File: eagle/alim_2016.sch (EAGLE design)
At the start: 52 parts, among them J1 AVR_SPI_PRG_6PTH, J2 AVR_SPI_PRG_6PTH, U1 3.3V, U2 LM2678S-5.0, U4 LM2596S-ADJ, U5 ATTINY85-20SU, U6 ATMEGA328P_TQFP

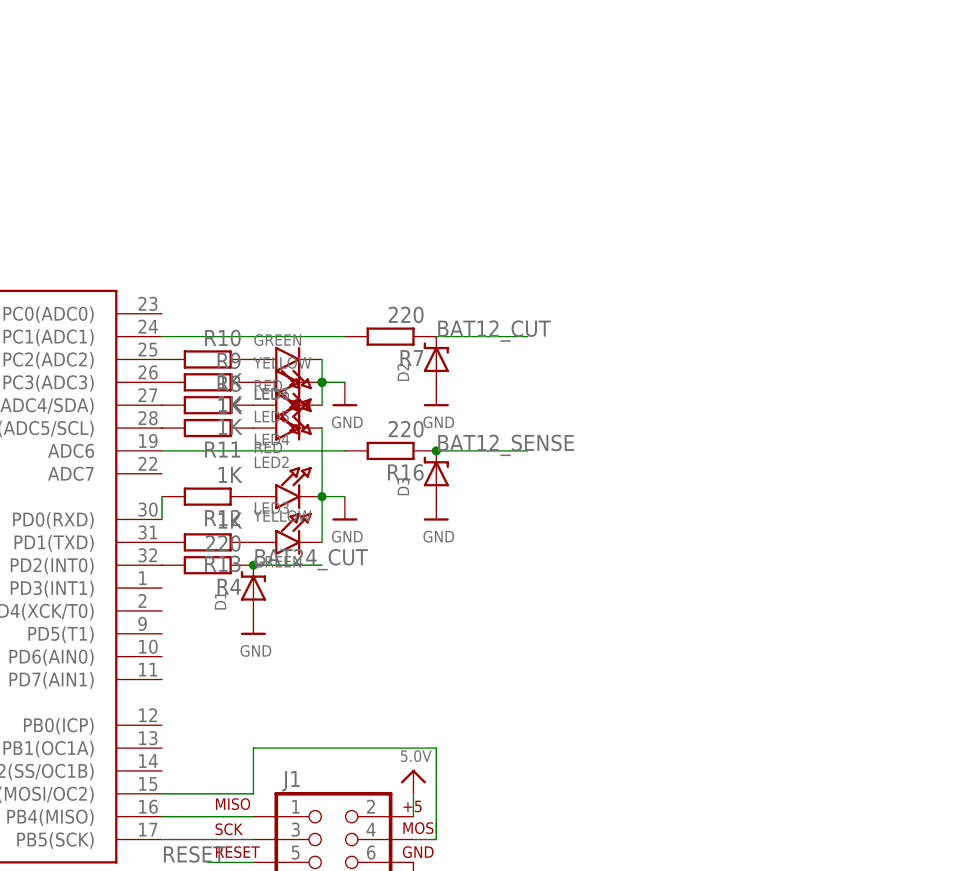
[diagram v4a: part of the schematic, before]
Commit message: adding other battery voltage sense
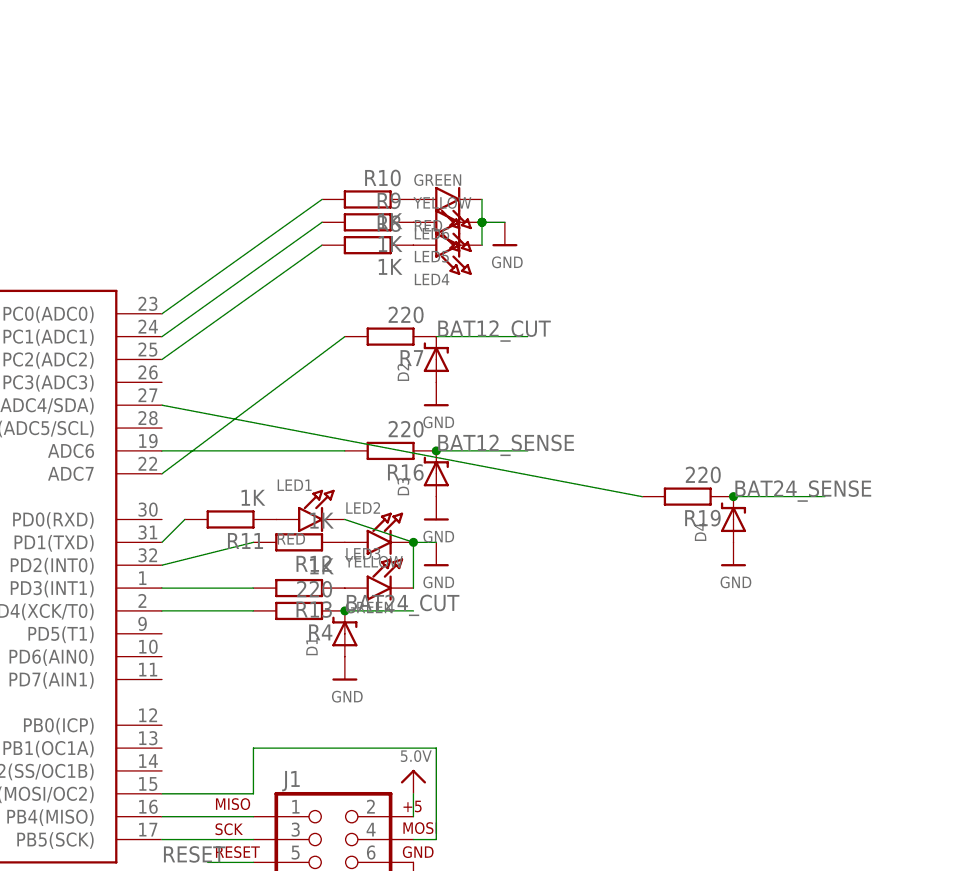
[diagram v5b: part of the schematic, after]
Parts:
- added D4: (no value), alim:DIODE-ZENERSOD123
- added R19: 220, resistor:R-EU_M0805
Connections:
- new net N$28: R19.2, U6.PC4(ADC4/SDA)
- net BAT24_SENSE: now also D4.C, R19.1
- net GND: now also D4.A
- net N$11: now also U6.PD4(XCK/T0); no longer U6.PD2(INT0)
- net N$14: now also R9.2; no longer R7.2
- net N$21: now also R8.2; no longer R10.2
- net N$22: now also R10.2, U6.PC0(ADC0); no longer R9.2, U6.PC3(ADC3)
- net N$23: now also R7.2, U6.ADC7; no longer R8.2, U6.PC4(ADC4/SDA)
- net N$24: now also U6.PD3(INT1); no longer U6.PD1(TXD)
- net N$25: now also U6.PD2(INT0); no longer U6.PD0(RXD)
- net N$26: now also U6.PD1(TXD); no longer U6.PC5(ADC5/SCL)
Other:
- moved on the sheet: D1, LED1, LED2, LED3, LED4, LED5, LED6, R10, R11, R12, R13, R4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
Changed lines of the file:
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@@
 <part name="R17" library="resistor" deviceset="R-EU_" device="M0805" value="1K"/>
 <part name="R18" library="resistor" deviceset="R-EU_" device="M0805" value="1K"/>
+<part name="D4" library="alim" deviceset="DIODE-ZENER" device="SOD123"/>
+<part name="R19" library="resistor" deviceset="R-EU_" device="M0805" value="220"/>
+<part name="U$28" library="microbuilder" deviceset="GND" device=""/>
 </parts>
 <sheets>
@@
 <instance part="12V" gate="-1" x="-2.54" y="43.18"/>
 <instance part="12V" gate="-2" x="-2.54" y="22.86"/>
-<instance part="LED1" gate="G$1" x="109.22" y="-93.98"/>
-<instance part="LED2" gate="G$1" x="109.22" y="-101.6"/>
-<instance part="LED3" gate="G$1" x="109.22" y="-106.68"/>
+<instance part="LED1" gate="G$1" x="111.76" y="-104.14"/>
+<instance part="LED2" gate="G$1" x="119.38" y="-106.68"/>
+<instance part="LED3" gate="G$1" x="119.38" y="-111.76"/>
 <instance part="LED7" gate="G$1" x="-12.7" y="25.4" rot="R270"/>
-<instance part="LED4" gate="G$1" x="109.22" y="-91.44" rot="MR180"/>
-<instance part="LED5" gate="G$1" x="109.22" y="-88.9" rot="MR180"/>
-<instance part="LED6" gate="G$1" x="109.22" y="-86.36" rot="MR180"/>
+<instance part="LED4" gate="G$1" x="127" y="-73.66" rot="MR180"/>
+<instance part="LED5" gate="G$1" x="127" y="-71.12" rot="MR180"/>
+<instance part="LED6" gate="G$1" x="127" y="-68.58" rot="MR180"/>
 <instance part="LED8" gate="G$1" x="5.08" y="-5.08" rot="R270"/>
 <instance part="R6" gate="G$1" x="-17.78" y="30.48" rot="R180"/>
 <instance part="R3" gate="G$1" x="0" y="0" rot="R180"/>
-<instance part="D1" gate="G$1" x="104.14" y="-111.76" rot="R90"/>
-<instance part="R4" gate="G$1" x="99.06" y="-109.22" rot="R180"/>
+<instance part="D1" gate="G$1" x="114.3" y="-116.84" rot="R90"/>
+<instance part="R4" gate="G$1" x="109.22" y="-114.3" rot="R180"/>
 <instance part="D2" gate="G$1" x="124.46" y="-86.36" rot="R90"/>
 <instance part="R7" gate="G$1" x="119.38" y="-83.82" rot="R180"/>
 <instance part="U$6" gate="G$1" x="124.46" y="-91.44"/>
-<instance part="U$18" gate="G$1" x="104.14" y="-116.84"/>
-<instance part="R8" gate="G$1" x="99.06" y="-91.44" rot="MR0"/>
-<instance part="R9" gate="G$1" x="99.06" y="-88.9" rot="MR0"/>
-<instance part="R10" gate="G$1" x="99.06" y="-86.36" rot="MR0"/>
-<instance part="R11" gate="G$1" x="99.06" y="-93.98" rot="R180"/>
-<instance part="R12" gate="G$1" x="99.06" y="-101.6" rot="R180"/>
-<instance part="R13" gate="G$1" x="99.06" y="-106.68" rot="R180"/>
-<instance part="U$26" gate="G$1" x="114.3" y="-104.14"/>
+<instance part="U$18" gate="G$1" x="114.3" y="-121.92"/>
+<instance part="R8" gate="G$1" x="116.84" y="-73.66" rot="MR0"/>
+<instance part="R9" gate="G$1" x="116.84" y="-71.12" rot="MR0"/>
+<instance part="R10" gate="G$1" x="116.84" y="-68.58" rot="MR0"/>
+<instance part="R11" gate="G$1" x="101.6" y="-104.14" rot="R180"/>
+<instance part="R12" gate="G$1" x="109.22" y="-106.68" rot="R180"/>
+<instance part="R13" gate="G$1" x="109.22" y="-111.76" rot="R180"/>
+<instance part="U$26" gate="G$1" x="124.46" y="-109.22"/>
 <instance part="U6" gate="U$1" x="71.12" y="-111.76"/>
 <instance part="R14" gate="G$1" x="-5.08" y="38.1" rot="R90"/>
@@
 <instance part="D3" gate="G$1" x="124.46" y="-99.06" rot="R90"/>
 <instance part="R16" gate="G$1" x="119.38" y="-96.52" rot="R180"/>
-<instance part="U$25" gate="G$1" x="114.3" y="-91.44"/>
+<instance part="U$25" gate="G$1" x="132.08" y="-73.66"/>
 <instance part="U$27" gate="G$1" x="124.46" y="-104.14"/>
 <instance part="R17" gate="G$1" x="-25.4" y="7.62" rot="R90"/>
 <instance part="R18" gate="G$1" x="-25.4" y="-2.54" rot="R90"/>
+<instance part="D4" gate="G$1" x="157.48" y="-104.14" rot="R90"/>
+<instance part="R19" gate="G$1" x="152.4" y="-101.6" rot="R180"/>
+<instance part="U$28" gate="G$1" x="157.48" y="-109.22"/>
 </instances>
 <busses>
@@
 <pinref part="LED3" gate="G$1" pin="C"/>
 <pinref part="LED2" gate="G$1" pin="C"/>
-<wire x1="111.76" y1="-106.68" x2="111.76" y2="-101.6" width="0.1524" layer="91"/>
+<wire x1="121.92" y1="-111.76" x2="121.92" y2="-106.68" width="0.1524" layer="91"/>
 <pinref part="LED1" gate="G$1" pin="C"/>
-<wire x1="111.76" y1="-101.6" x2="111.76" y2="-93.98" width="0.1524" layer="91"/>
+<wire x1="121.92" y1="-106.68" x2="114.3" y2="-104.14" width="0.1524" layer="91"/>
 <pinref part="U$26" gate="G$1" pin="GND"/>
-<wire x1="114.3" y1="-101.6" x2="111.76" y2="-101.6" width="0.1524" layer="91"/>
-<junction x="111.76" y="-101.6"/>
+<wire x1="124.46" y1="-106.68" x2="121.92" y2="-106.68" width="0.1524" layer="91"/>
+<junction x="121.92" y="-106.68"/>
 </segment>
 <segment>
 <pinref part="LED4" gate="G$1" pin="C"/>
 <pinref part="LED6" gate="G$1" pin="C"/>
-<wire x1="111.76" y1="-91.44" x2="111.76" y2="-88.9" width="0.1524" layer="91"/>
+<wire x1="129.54" y1="-73.66" x2="129.54" y2="-71.12" width="0.1524" layer="91"/>
 <pinref part="LED5" gate="G$1" pin="C"/>
-<junction x="111.76" y="-88.9"/>
-<junction x="111.76" y="-88.9"/>
-<wire x1="111.76" y1="-88.9" x2="111.76" y2="-86.36" width="0.1524" layer="91"/>
+<junction x="129.54" y="-71.12"/>
+<junction x="129.54" y="-71.12"/>
+<wire x1="129.54" y1="-71.12" x2="129.54" y2="-68.58" width="0.1524" layer="91"/>
 <pinref part="U$25" gate="G$1" pin="GND"/>
-<wire x1="111.76" y1="-88.9" x2="114.3" y2="-88.9" width="0.1524" layer="91"/>
+<wire x1="129.54" y1="-71.12" x2="132.08" y2="-71.12" width="0.1524" layer="91"/>
 </segment>
 <segment>
 <pinref part="D3" gate="G$1" pin="A"/>
 <pinref part="U$27" gate="G$1" pin="GND"/>
+</segment>
+<segment>
+<pinref part="D4" gate="G$1" pin="A"/>
+<pinref part="U$28" gate="G$1" pin="GND"/>
 </segment>
 </net>
@@
 </segment>
 <segment>
-<label x="104.14" y="-109.22" size="1.778" layer="95"/>
+<label x="114.3" y="-114.3" size="1.778" layer="95"/>
 <pinref part="D1" gate="G$1" pin="C"/>
-<wire x1="111.76" y1="-109.22" x2="104.14" y2="-109.22" width="0.1524" layer="91"/>
+<wire x1="121.92" y1="-114.3" x2="114.3" y2="-114.3" width="0.1524" layer="91"/>
 <pinref part="R4" gate="G$1" pin="1"/>
-<junction x="104.14" y="-109.22"/>
+<junction x="114.3" y="-114.3"/>
 </segment>
 </net>
@@
 </segment>
 </net>
-<net name="N$11" class="0">
-<segment>
-<pinref part="R4" gate="G$1" pin="2"/>
-<pinref part="U6" gate="U$1" pin="PD2(INT0)"/>
-</segment>
-</net>
-<net name="N$14" class="0">
-<segment>
-<pinref part="R7" gate="G$1" pin="2"/>
-<pinref part="U6" gate="U$1" pin="PC1(ADC1)"/>
-<wire x1="114.3" y1="-83.82" x2="93.98" y2="-83.82" width="0.1524" layer="91"/>
-</segment>
-</net>
-<net name="N$21" class="0">
-<segment>
-<pinref part="U6" gate="U$1" pin="PC2(ADC2)"/>
-<pinref part="R10" gate="G$1" pin="2"/>
-</segment>
-</net>
-<net name="N$22" class="0">
-<segment>
-<pinref part="U6" gate="U$1" pin="PC3(ADC3)"/>
-<pinref part="R9" gate="G$1" pin="2"/>
-</segment>
-</net>
-<net name="N$23" class="0">
-<segment>
-<pinref part="U6" gate="U$1" pin="PC4(ADC4/SDA)"/>
-<pinref part="R8" gate="G$1" pin="2"/>
-</segment>
-</net>
-<net name="N$24" class="0">
-<segment>
-<pinref part="U6" gate="U$1" pin="PD1(TXD)"/>
-<pinref part="R13" gate="G$1" pin="2"/>
-</segment>
-</net>
-<net name="N$25" class="0">
-<segment>
-<pinref part="U6" gate="U$1" pin="PD0(RXD)"/>
-<pinref part="R12" gate="G$1" pin="2"/>
-<wire x1="93.98" y1="-104.14" x2="93.98" y2="-101.6" width="0.1524" layer="91"/>
-</segment>
-</net>
-<net name="N$26" class="0">
-<segment>
-<pinref part="U6" gate="U$1" pin="PC5(ADC5/SCL)"/>
-<pinref part="R11" gate="G$1" pin="2"/>
-</segment>
-</net>
 <net name="BAT12_SENSE" class="0">
 <segment>
@@
 <label x="-25.4" y="2.54" size="1.778" layer="95"/>
 </segment>
-</net>
+<segment>
+<label x="157.48" y="-101.6" size="1.778" layer="95"/>
+<pinref part="D4" gate="G$1" pin="C"/>
+<wire x1="157.48" y1="-101.6" x2="167.64" y2="-101.6" width="0.1524" layer="91"/>
+<pinref part="R19" gate="G$1" pin="1"/>
+<junction x="157.48" y="-101.6"/>
+</segment>
+</net>
+<net name="N$23" class="0">
+<segment>
+<pinref part="U6" gate="U$1" pin="ADC7"/>
+<pinref part="R7" gate="G$1" pin="2"/>
+<wire x1="93.98" y1="-99.06" x2="114.3" y2="-83.82" width="0.1524" layer="91"/>
+</segment>
+</net>
+<net name="N$28" class="0">
+<segment>
+<pinref part="U6" gate="U$1" pin="PC4(ADC4/SDA)"/>
+<pinref part="R19" gate="G$1" pin="2"/>
+<wire x1="93.98" y1="-91.44" x2="147.32" y2="-101.6" width="0.1524" layer="91"/>
+</segment>
+</net>
+<net name="N$22" class="0">
+<segment>
+<pinref part="U6" gate="U$1" pin="PC0(ADC0)"/>
+<pinref part="R10" gate="G$1" pin="2"/>
+<wire x1="93.98" y1="-81.28" x2="111.76" y2="-68.58" width="0.1524" layer="91"/>
+</segment>
+</net>
+<net name="N$14" class="0">
+<segment>
+<pinref part="U6" gate="U$1" pin="PC1(ADC1)"/>
+<pinref part="R9" gate="G$1" pin="2"/>
+<wire x1="93.98" y1="-83.82" x2="111.76" y2="-71.12" width="0.1524" layer="91"/>
+</segment>
+</net>
+<net name="N$21" class="0">
+<segment>
+<pinref part="U6" gate="U$1" pin="PC2(ADC2)"/>
+<pinref part="R8" gate="G$1" pin="2"/>
+<wire x1="93.98" y1="-86.36" x2="111.76" y2="-73.66" width="0.1524" layer="91"/>
+</segment>
+</net>
+<net name="N$11" class="0">
+<segment>
+<pinref part="U6" gate="U$1" pin="PD4(XCK/T0)"/>
+<pinref part="R4" gate="G$1" pin="2"/>
+<wire x1="93.98" y1="-114.3" x2="104.14" y2="-114.3" width="0.1524" layer="91"/>
+</segment>
+</net>
+<net name="N$24" class="0">
+<segment>
+<pinref part="U6" gate="U$1" pin="PD3(INT1)"/>
+<pinref part="R13" gate="G$1" pin="2"/>
+<wire x1="93.98" y1="-111.76" x2="104.14" y2="-111.76" width="0.1524" layer="91"/>
+</segment>
+</net>
+<net name="N$25" class="0">
+<segment>
+<pinref part="U6" gate="U$1" pin="PD2(INT0)"/>
+<pinref part="R12" gate="G$1" pin="2"/>
+<wire x1="93.98" y1="-109.22" x2="104.14" y2="-106.68" width="0.1524" layer="91"/>
+</segment>
+</net>
+<net name="N$26" class="0">
+<segment>
+<pinref part="U6" gate="U$1" pin="PD1(TXD)"/>
+<pinref part="R11" gate="G$1" pin="2"/>
+<wire x1="93.98" y1="-106.68" x2="96.52" y2="-104.14" width="0.1524" layer="91"/>
+</segment>
+</net>
